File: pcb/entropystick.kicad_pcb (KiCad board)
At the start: 2 copper layers, 25 parts, among them IC1 ICE40LP384-SG32, J1 USB_A, J2 TC2050, J3 Conn_02x04_Odd_Even, U1 CP2102-QFN28, U2 AT25DF256-XMHN-T, U3 MIC5365-1.2YC5, Y1 XO32

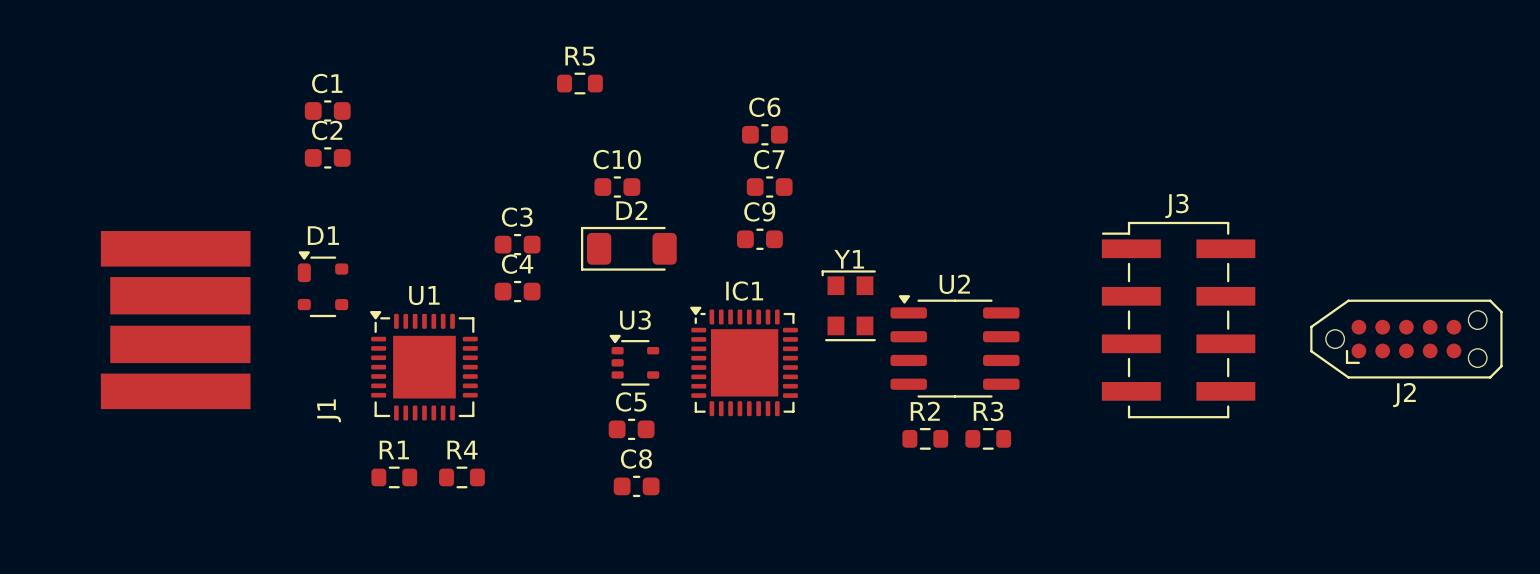
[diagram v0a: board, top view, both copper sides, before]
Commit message: improve pin assignments, place&route
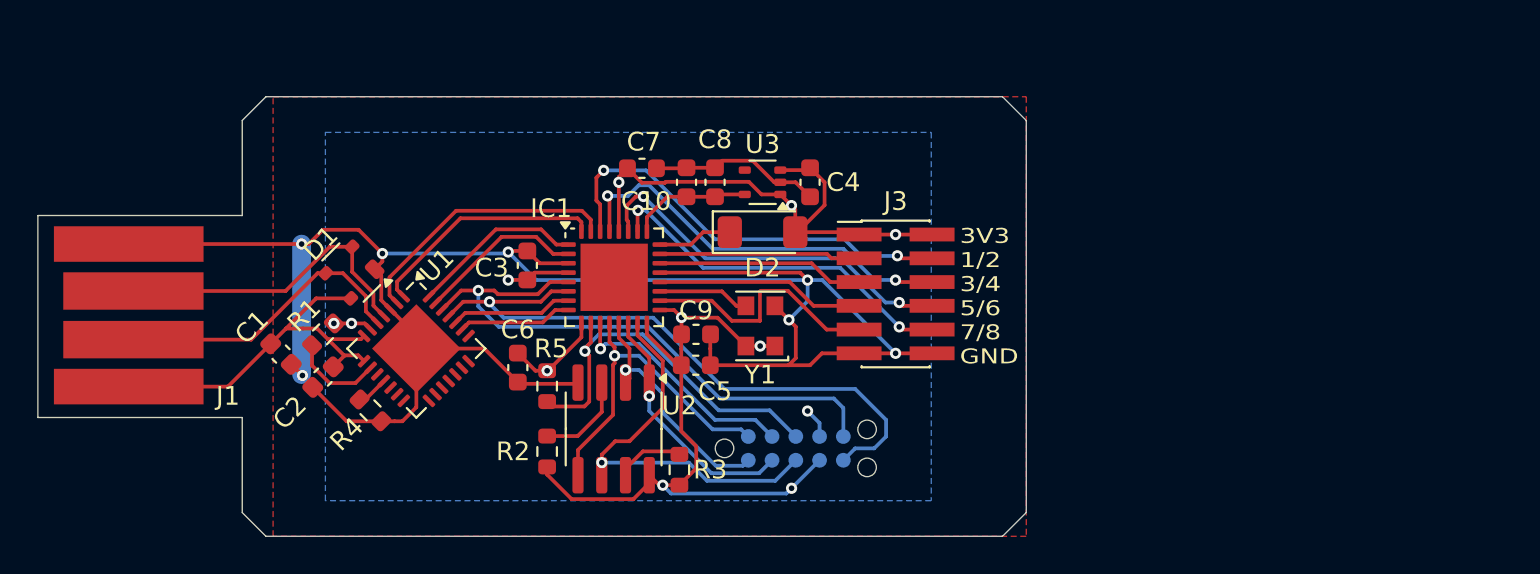
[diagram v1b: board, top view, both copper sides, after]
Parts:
- J2: moved to B.Cu
- J3: value Conn_02x04_Odd_Even -> Conn_02x06_Odd_Even; footprint Connector_PinHeader_2.54mm:PinHeader_2x04_P2.54mm_Vertical_SMD -> Connector_PinHeader_1.27mm:PinHeader_2x06_P1.27mm_Vertical_SMD
- moved J2 33.2 mm to (161.7, 107.7)
- moved R2 20.2 mm to (148.4, 107.9), turned to 90 degrees
- moved U2 18.7 mm to (151.9, 106.7), turned to -90 degrees
- moved C6 18.1 mm to (146.8, 103.4), turned to -90 degrees
- moved C8 16.8 mm to (157.4, 93.5), turned to 90 degrees
- moved C4 16.7 mm to (162.4, 93.5), turned to -90 degrees
- moved R3 16.6 mm to (155.4, 108.8), turned to 90 degrees
- moved R5 16.3 mm to (148.4, 104.4), turned to -90 degrees
- moved J3 15.2 mm to (167.0, 99.4)
- moved C1 13.2 mm to (134.2, 102.7), turned to -45 degrees
- moved U3 11.8 mm to (159.9, 93.5), turned to 180 degrees
- moved C2 11.7 mm to (136.4, 103.9), turned to -135 degrees
- moved R1 8.55 mm to (136.4, 101.6), turned to -135 degrees
- moved IC1 8.34 mm to (152.0, 98.6)
- moved D2 7.04 mm to (159.9, 96.1)
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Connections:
- IC1 pad 1: /UART_TXD -> /UART_DTR
- IC1 pad 18: /UART_DCD -> /GPIO7
- IC1 pad 19: /UART_RI -> /CLK32M
- IC1 pad 2: /UART_RXD -> /UART_DSR
- IC1 pad 20: /CLK32M -> /GPIO5
- IC1 pad 22: /GPIO1 -> /GPIO3
- IC1 pad 23: /GPIO2 -> /GPIO1
- IC1 pad 26: /GPIO3 -> /GPIO8
- IC1 pad 27: /GPIO4 -> /GPIO6
- IC1 pad 29: /GPIO5 -> /GPIO4
- IC1 pad 30: /GPIO6 -> /GPIO2
- IC1 pad 31: /GPIO7 -> /UART_RI
- IC1 pad 32: /GPIO8 -> /UART_DCD
- IC1 pad 5: /UART_RTS -> /UART_TXD
- IC1 pad 6: /UART_CTS -> /UART_RXD
- IC1 pad 7: /UART_DSR -> /UART_RTS
- IC1 pad 8: /UART_DTR -> /UART_CTS
- J3 pad 1: /GPIO1 -> +3V3
- J3 pad 2: /GPIO2 -> +3V3
- J3 pad 3: /GPIO3 -> /GPIO1
- J3 pad 4: /GPIO4 -> /GPIO2
- J3 pad 5: /GPIO5 -> /GPIO3
- J3 pad 6: /GPIO6 -> /GPIO4
- J3 pad 7: /GPIO7 -> /GPIO5
- J3 pad 8: /GPIO8 -> /GPIO6
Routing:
- net GND: track 0.00 -> 119.8 mm, vias 0 -> 8
- net +3V3: track 0.00 -> 77.1 mm, vias 0 -> 11
- net /UART_RXD: track 0.00 -> 34.5 mm, vias 0 -> 1
- net /UART_TXD: track 0.00 -> 31.7 mm, vias 0 -> 1
- net /GPIO2: track 0.00 -> 23.0 mm, vias 0 -> 2
- net /GPIO4: track 0.00 -> 21.7 mm, vias 0 -> 2
- net VBUS: track 0.00 -> 21.6 mm
- net /SCK: track 0.00 -> 21.0 mm, vias 0 -> 1
- net /CRESET_B: track 0.00 -> 20.9 mm, vias 0 -> 1
- net /GPIO6: track 0.00 -> 20.4 mm, vias 0 -> 2
- net /GPIO8: track 0.00 -> 19.5 mm, vias 0 -> 2
- net /SDO: track 0.00 -> 18.1 mm, vias 0 -> 1
- net /DP: track 0.00 -> 17.1 mm
- net /DN: track 0.00 -> 16.1 mm
- net /UART_RI: track 0.00 -> 14.6 mm
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- added copper zone on B.Cu, net +3V3
- added copper zone on F.Cu, net GND
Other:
- board outline added: 52.8 x 23.5 mm
- board text added: "3V3 1/2 3/4 5/6 7/8 GND"
- board text added: "3v3"
- board text added: "GND"

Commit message: improve PCB
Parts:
- added D2: LED, LED_SMD:LED_0603_1608Metric, F.Cu at (146.2, 92.7)
- added D4: LED, LED_SMD:LED_0603_1608Metric, F.Cu at (159.4, 104.9)
- added R5: 1k, Resistor_SMD:R_0603_1608Metric, F.Cu at (149.2, 92.7)
- added R6: 1k, Resistor_SMD:R_0603_1608Metric, F.Cu at (156.3, 104.9)
- J3: footprint Connector_PinHeader_1.27mm:PinHeader_2x06_P1.27mm_Vertical_SMD -> Connector_PinHeader_2.54mm:PinHeader_2x06_P2.54mm_Vertical
- moved J3 5.91 mm to (169.8, 94.2)
- moved Y1 1.51 mm to (161.3, 101.2)
- moved C4 0.13 mm to (162.4, 93.3), turned to 90 degrees
- moved U3 0.13 mm to (159.9, 93.3)
- renumbered D2 to D3, R5 to R7
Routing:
- net GND: track 119.8 -> 150.3 mm, vias 8 -> 7
- net +3V3: track 77.1 -> 87.0 mm, vias 11 -> 14
- net /GPIO7: track 13.5 -> 19.7 mm
- net /GPIO5: track 11.2 -> 17.2 mm
- net /GPIO8: track 19.5 -> 25.2 mm, vias 2 -> 1
- net /GPIO6: track 20.4 -> 25.5 mm, vias 2 -> 1
- net /GPIO3: track 11.1 -> 16.0 mm
- net /GPIO1: track 10.7 -> 15.6 mm
- net /GPIO4: track 21.7 -> 26.3 mm, vias 2 -> 1
- net /GPIO2: track 23.0 -> 27.1 mm, vias 2 -> 1
- net /DN: track 16.1 -> 18.1 mm
- net /CLK32M: track 4.91 -> 6.42 mm
- net Net-(D4-A): track 0.00 -> 1.44 mm
- net Net-(D2-A): track 0.00 -> 1.44 mm
- net VBUS: track 21.6 -> 22.9 mm
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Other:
- board size 52.8 x 23.5 mm -> 56.6 x 23.5 mm
- board text added: "UART384 v1.0"
- board text added: "by dpiegdon"

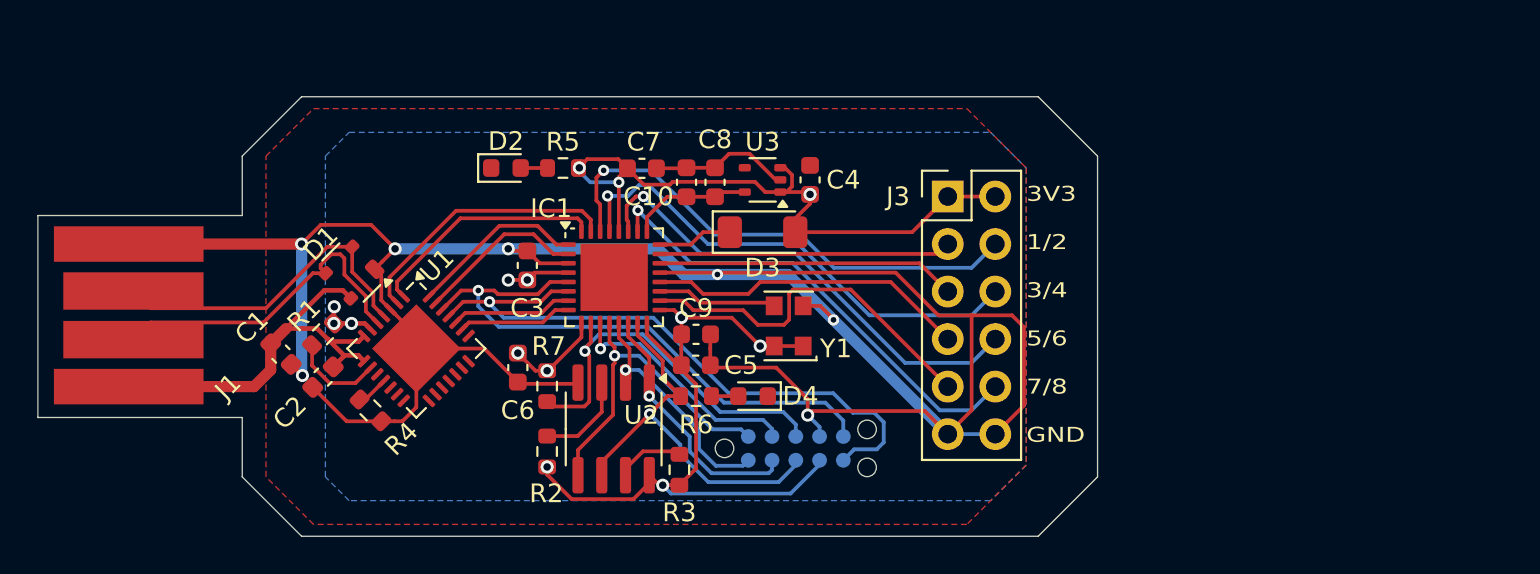
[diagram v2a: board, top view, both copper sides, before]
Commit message: add switch, LED; verify USB connector dimensions
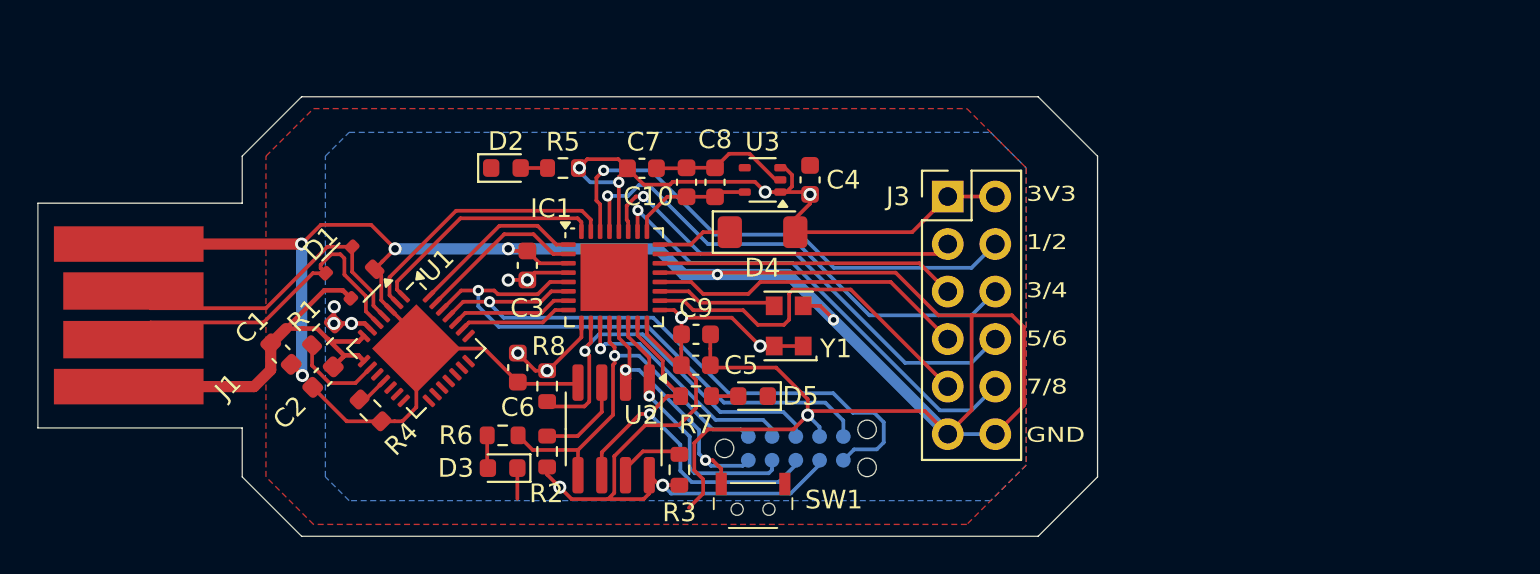
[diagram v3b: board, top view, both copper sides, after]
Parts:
- added D3: LED, LED_SMD:LED_0603_1608Metric, F.Cu at (146.0, 108.8)
- added R6: 1k, Resistor_SMD:R_0603_1608Metric, F.Cu at (146.0, 107.0)
- added SW1: SW_Push, dpiegdon:TS-1224W_Side_Button_2x4x3.3mm_3.5mm_3.8mm_SMD_Aliexpress, F.Cu at (159.4, 111.0)
- renumbered D3 to D4, D4 to D5, R6 to R7, R7 to R8
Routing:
- net GND: track 150.3 -> 162.6 mm
- net +3V3: track 87.0 -> 90.7 mm, vias 14 -> 15
- net /SDO: track 18.1 -> 21.6 mm
- net /SDI: track 12.9 -> 14.9 mm, vias 1 -> 2
- net Net-(D3-A): track 0.00 -> 1.77 mm
- net /SCK: track 21.5 -> 22.3 mm
- net /SS: track 13.0 -> 13.5 mm
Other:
- outline, holes or cut-outs redrawn
